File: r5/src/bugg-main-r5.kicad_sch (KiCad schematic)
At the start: 44 parts, among them T14 , T15 , T16 , T3 , T39 , T40 , U1 74LVC1G07DCK, U34 74LVC1G157GV

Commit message: Change 0805 47uF to 1206 to save a BOM line. Update layout, DRC pass.
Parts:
- C53: MPN (none) -> GRM155R71H104KE14D; Manufacturer (none) -> Murata; Mouser (none) -> 81-GRM155R71H104KE4D; Voltage (none) -> 50V

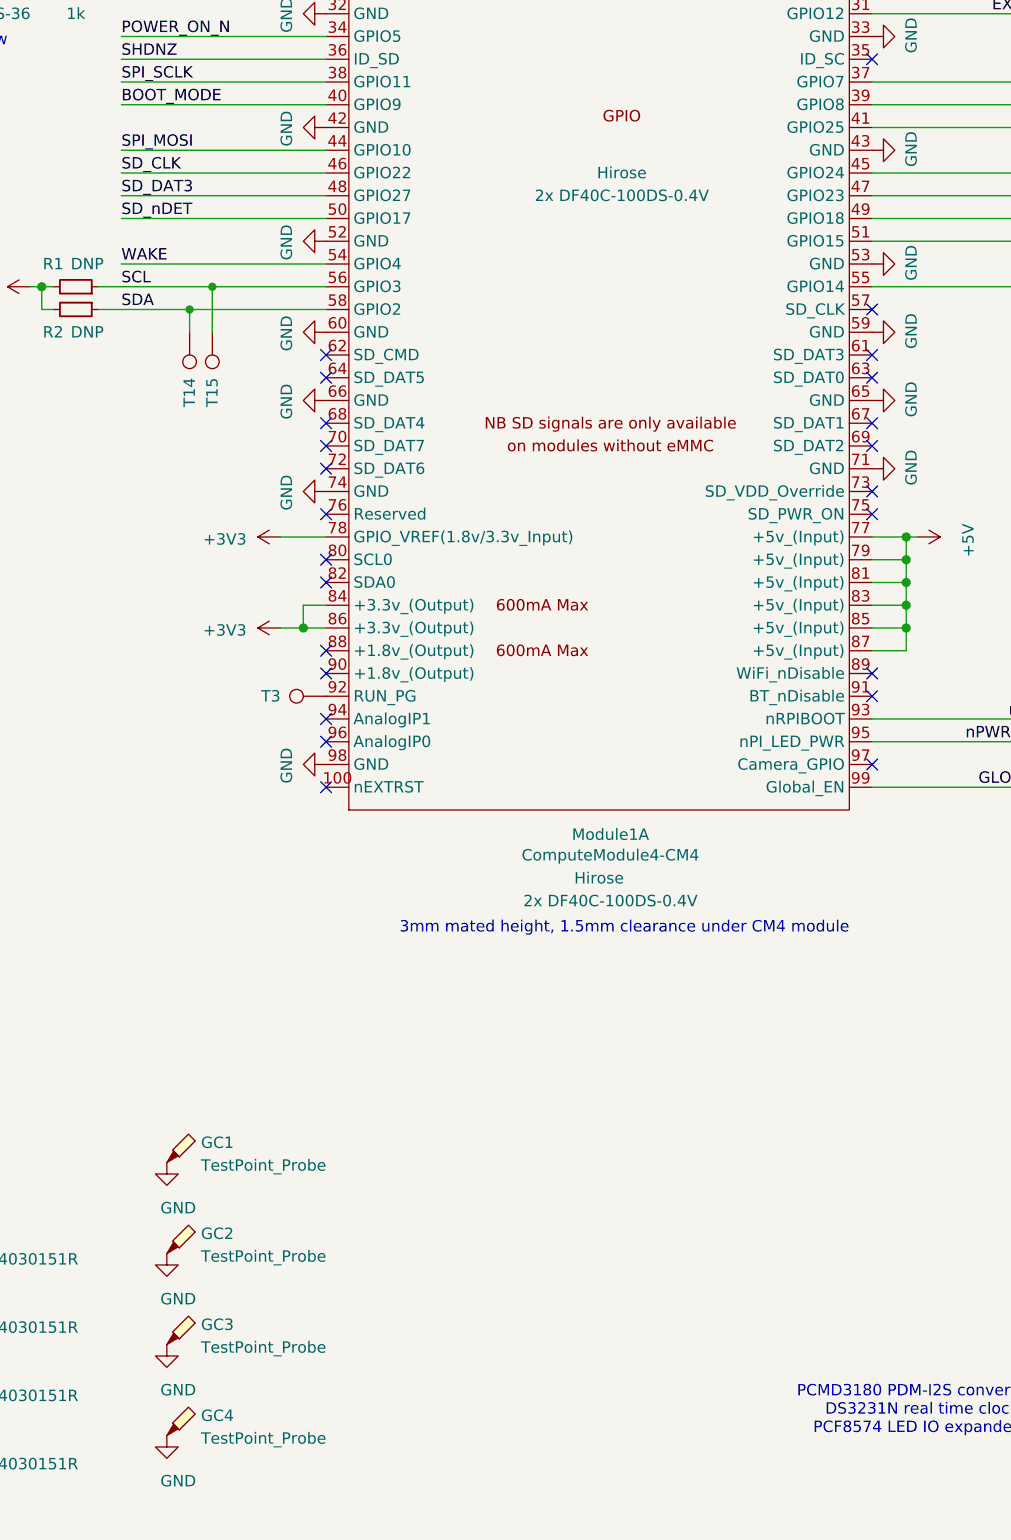
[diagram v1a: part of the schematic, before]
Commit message: Oops, hadn't run the ERC for ages. Ran, passed. Add ERC and DRC exclusions where unavoidable
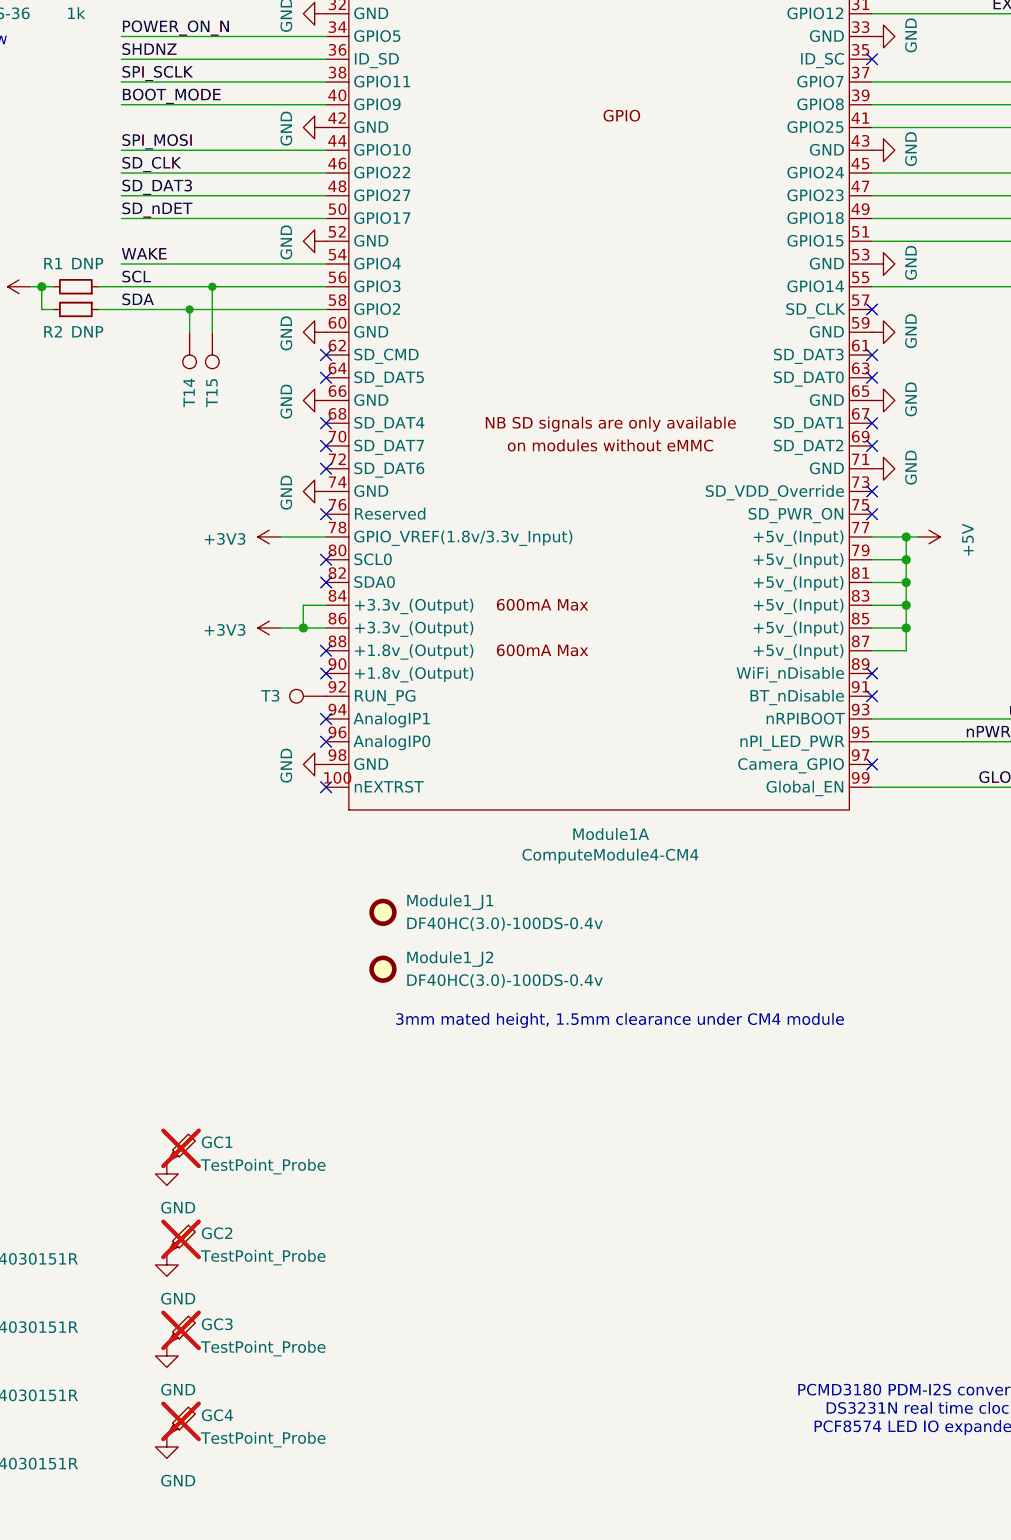
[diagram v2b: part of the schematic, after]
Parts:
- added Module1_J1, Module1_J2: DF40HC(3.0)-100DS-0.4v, symbol Mechanical:Fiducial
- D1: Digikey (none) -> 475-1410-6-ND; MPN (none) -> LGR971-KN-1; Manufacturer (none) -> Osram; Mouser (none) -> 720-LGR971-KN-1
- D2: Digikey (none) -> 475-1415-6-ND; MPN (none) -> LHR974-LP-1; Manufacturer (none) -> Osram; Mouser (none) -> 720-LHR974-LP-1
- D7: Digikey (none) -> 475-2560-6-ND; MPN (none) -> LYR976-PS-36; Manufacturer (none) -> Osram; Mouser (none) -> 720-LYR976-PS-36
- GC1, GC2, GC3, GC4: now not fitted
- Module1: Farnell (none) -> 3563481; Field4 Hirose -> (none); Field5 2x DF40C-100DS-0.4V -> (none); MPN (none) -> CM4002016; Manufacturer (none) -> Raspberry Pi
- SP1, SP2, SP3, SP4: Digikey (none) -> 732-7083-6-ND; MPN (none) -> 9774030151R; Manufacturer (none) -> Wurth; Mouser (none) -> 710-9774030151R
- U1: Digikey (none) -> 296-26591-6-ND; MPN (none) -> SN74LVC1G07DCKT; Manufacturer (none) -> TI; Mouser (none) -> 595-SN74LVC1G07DCK3
- U34: MPN (none) -> 74LVC1G157GV; Manufacturer (none) -> Nexperia; Mouser (none) -> 771-74LVC1G157GVQ100

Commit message: Ground clip BoM data. (Though DNP for mass production, anyway)
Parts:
- GC1, GC2, GC3, GC4: MPN (none) -> 5019; Manufacturer (none) -> Keystone; Mouser (none) -> 534-5019
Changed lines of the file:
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@@
       (effects (font (size 1.27 1.27)) hide)
     )
-    (property "MPN" "" (at 161.29 270.51 0)
+    (property "MPN" "5019" (at 161.29 270.51 0)
       (effects (font (size 1.27 1.27)) hide)
     )
-    (property "Mouser" "" (at 161.29 270.51 0)
+    (property "Mouser" " 534-5019" (at 161.29 270.51 0)
       (effects (font (size 1.27 1.27)) hide)
     )
@@
       (effects (font (size 1.27 1.27)) hide)
     )
+    (property "Manufacturer" "Keystone" (at 161.29 270.51 0)
+      (effects (font (size 1.27 1.27)) hide)
+    )
     (pin "1")
     (instances
@@
       (effects (font (size 1.27 1.27)) hide)
     )
-    (property "MPN" "" (at 161.29 260.35 0)
+    (property "MPN" "5019" (at 161.29 260.35 0)
       (effects (font (size 1.27 1.27)) hide)
     )
-    (property "Mouser" "" (at 161.29 260.35 0)
+    (property "Mouser" " 534-5019" (at 161.29 260.35 0)
       (effects (font (size 1.27 1.27)) hide)
     )
@@
       (effects (font (size 1.27 1.27)) hide)
     )
+    (property "Manufacturer" "Keystone" (at 161.29 260.35 0)
+      (effects (font (size 1.27 1.27)) hide)
+    )
     (pin "1")
     (instances
@@
       (effects (font (size 1.27 1.27)) hide)
     )
-    (property "MPN" "" (at 161.29 250.19 0)
+    (property "MPN" "5019" (at 161.29 250.19 0)
       (effects (font (size 1.27 1.27)) hide)
     )
-    (property "Mouser" "" (at 161.29 250.19 0)
+    (property "Mouser" " 534-5019" (at 161.29 250.19 0)
       (effects (font (size 1.27 1.27)) hide)
     )
@@
       (effects (font (size 1.27 1.27)) hide)
     )
+    (property "Manufacturer" "Keystone" (at 161.29 250.19 0)
+      (effects (font (size 1.27 1.27)) hide)
+    )
     (pin "1")
     (instances
@@
       (effects (font (size 1.27 1.27)) hide)
     )
-    (property "MPN" "" (at 161.29 240.03 0)
+    (property "MPN" "5019" (at 161.29 240.03 0)
       (effects (font (size 1.27 1.27)) hide)
     )
-    (property "Mouser" "" (at 161.29 240.03 0)
+    (property "Mouser" " 534-5019" (at 161.29 240.03 0)
       (effects (font (size 1.27 1.27)) hide)
     )
@@
       (effects (font (size 1.27 1.27)) hide)
     )
+    (property "Manufacturer" "Keystone" (at 161.29 240.03 0)
+      (effects (font (size 1.27 1.27)) hide)
+    )

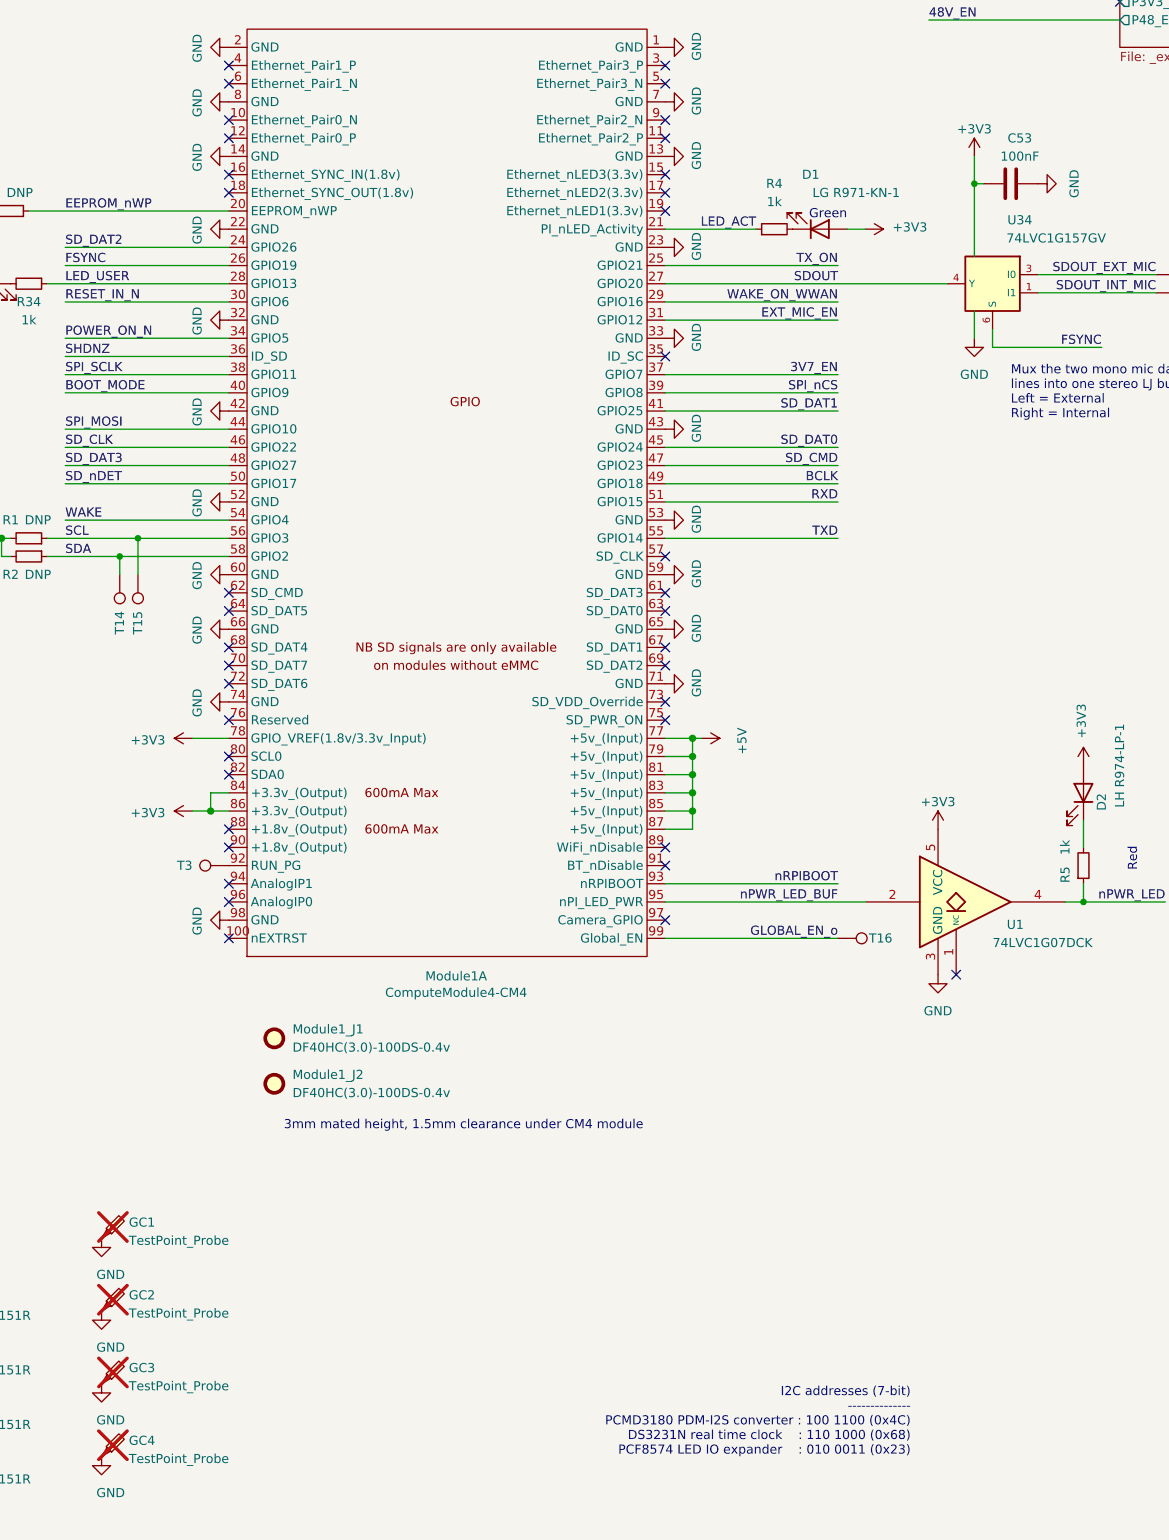
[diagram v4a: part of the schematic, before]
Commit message: Update to new Kicad nightly - file format update
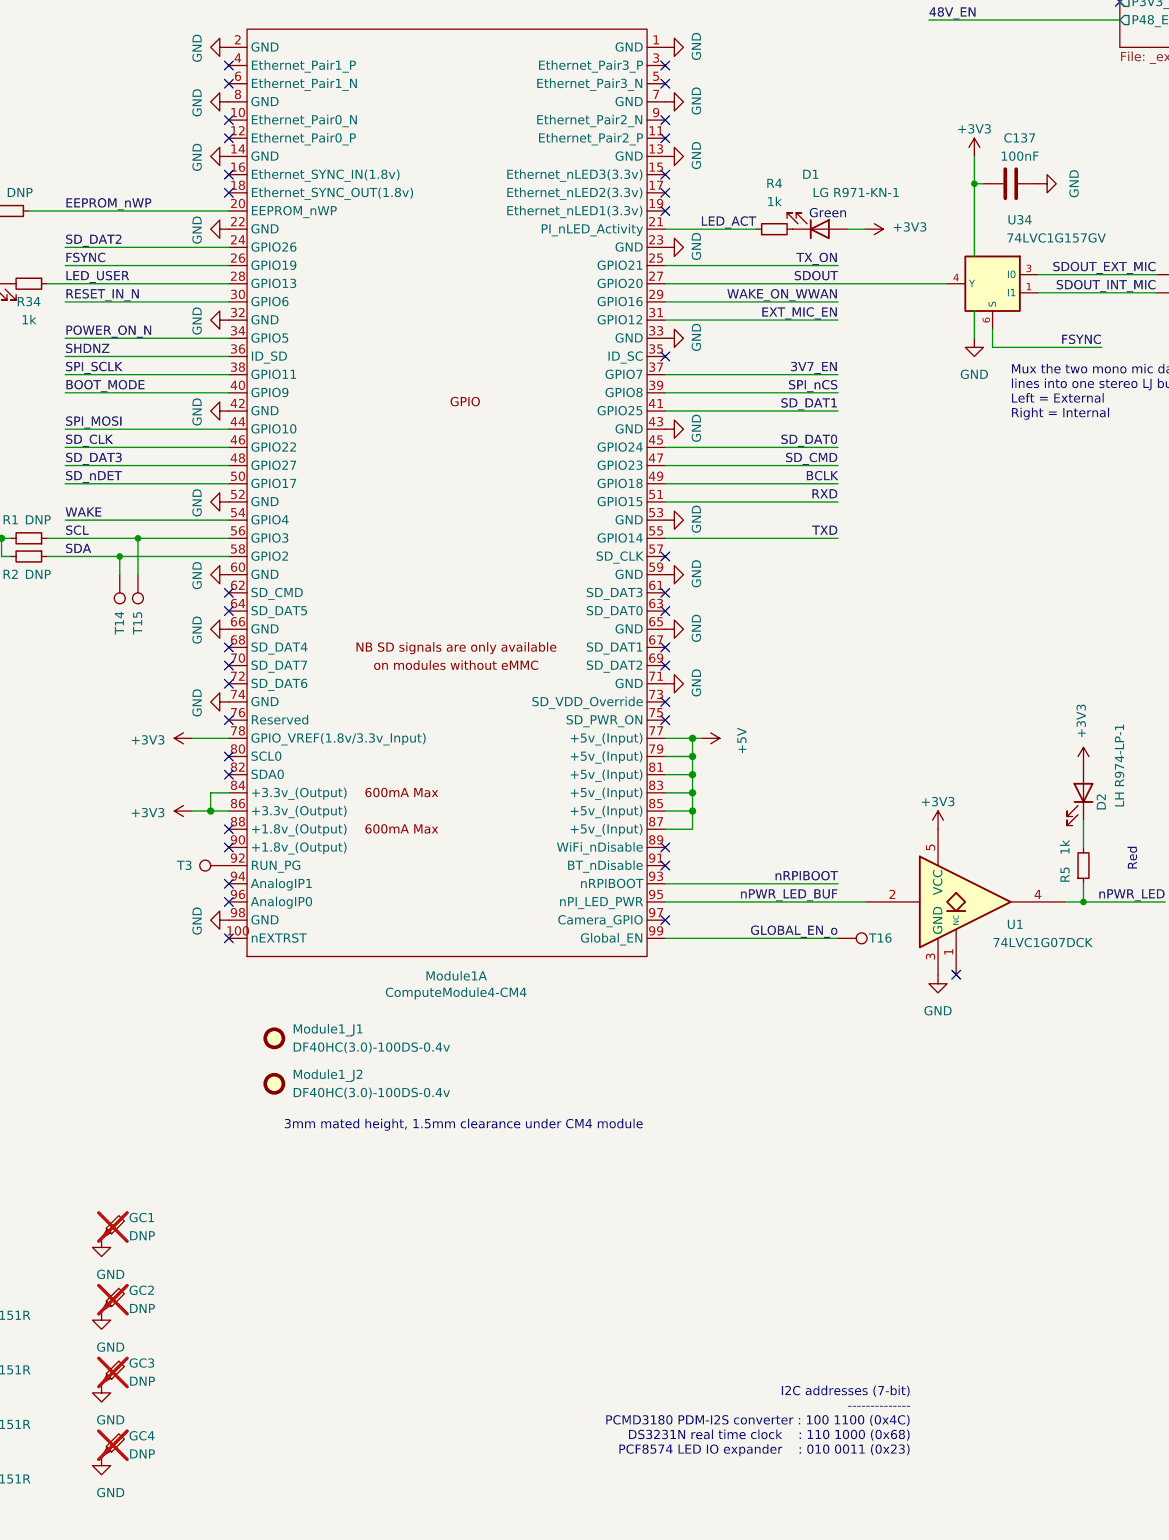
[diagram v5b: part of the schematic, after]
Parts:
- GC1, GC2, GC3, GC4: value TestPoint_Probe -> DNP
- renumbered C53 to C137
